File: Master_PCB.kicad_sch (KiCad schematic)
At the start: 15 parts, among them J1 Conn_01x10_Female, J2 Conn_01x04_Female, J214 Conn_01x02_Male, J215 Conn_01x03_Male, J216 Conn_01x02_Male, J220 Conn_01x02_Male, J221 Conn_01x03_Male, J3 Conn_01x06_Female, J4 SJ1-3533NG

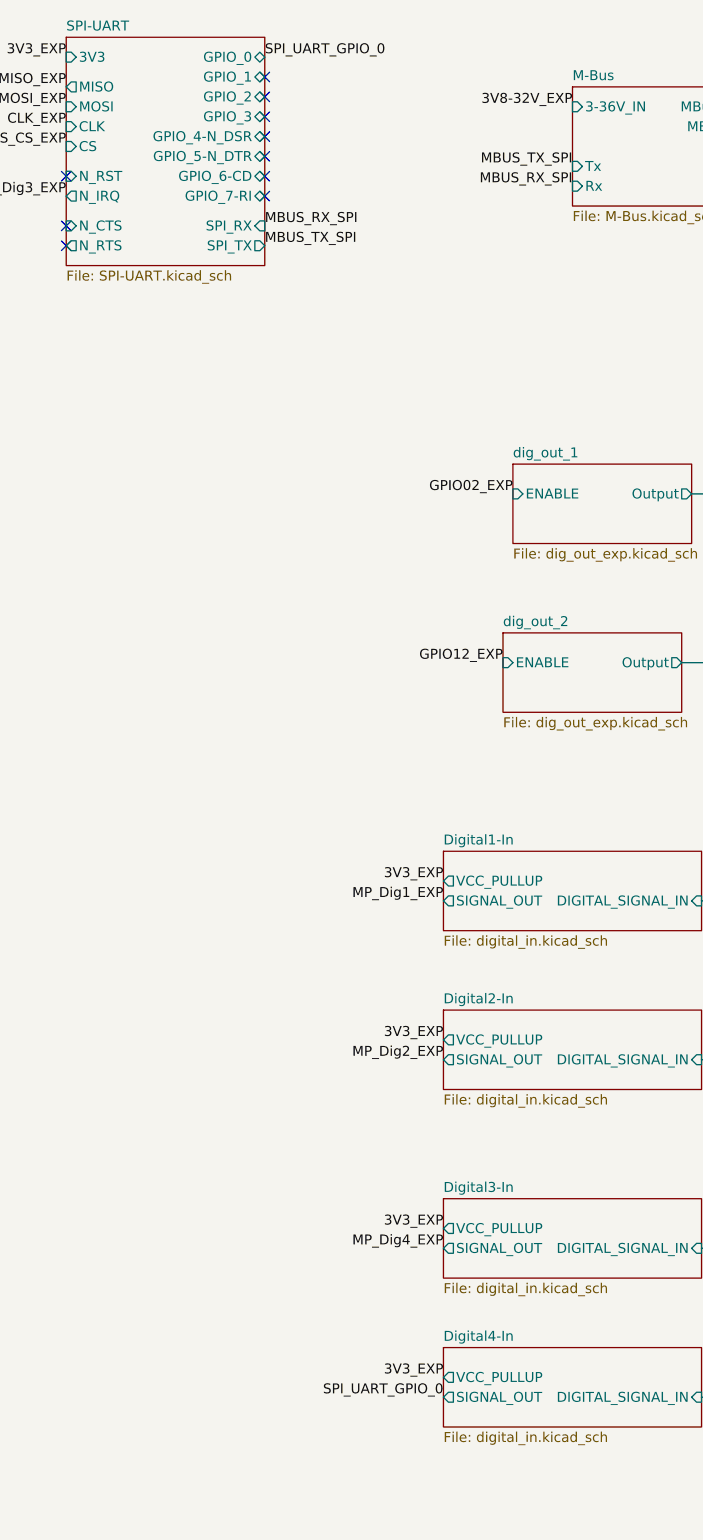
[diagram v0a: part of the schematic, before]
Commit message: changed pin of digital in 1 to a GPIO to be able to handel a serial connection
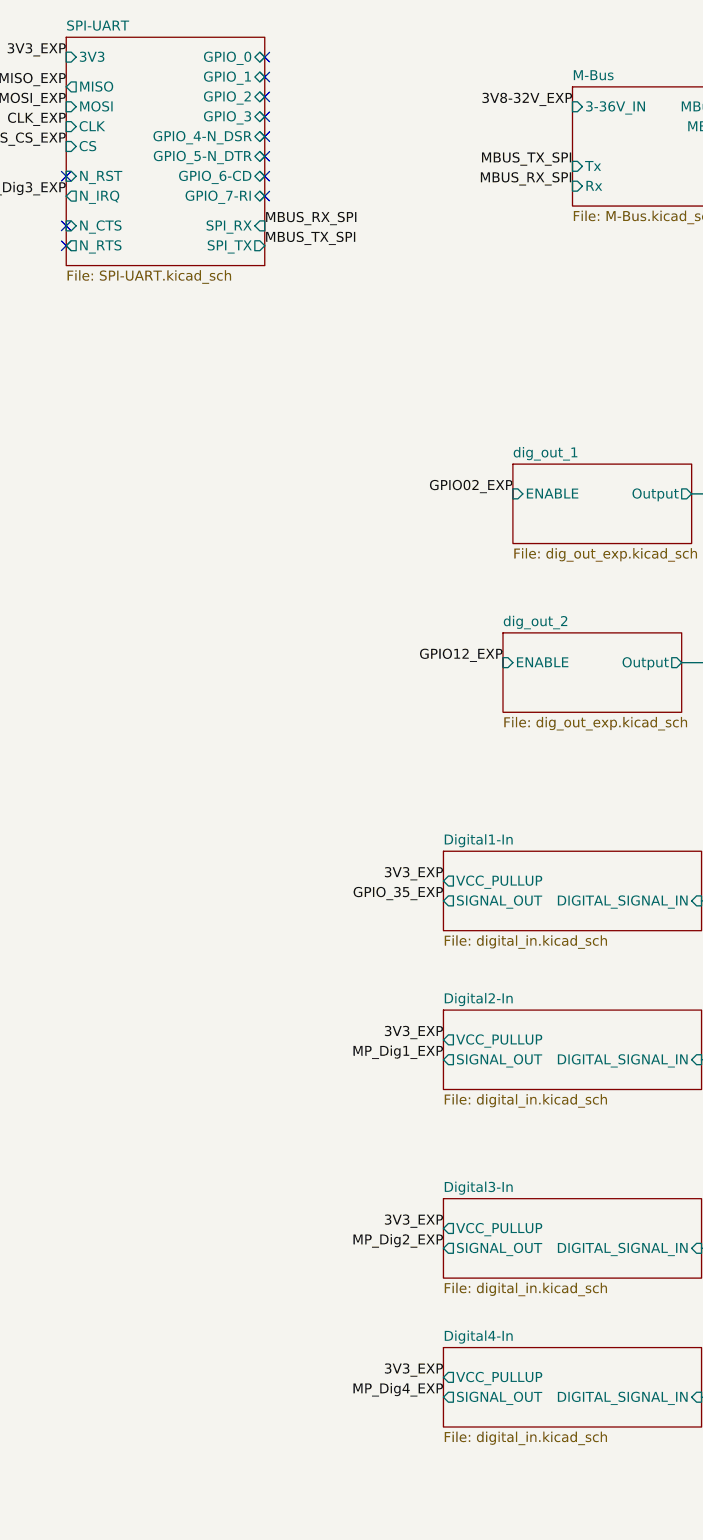
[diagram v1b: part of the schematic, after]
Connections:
- no-connect marks 11 -> 12
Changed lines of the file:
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@@
+	)
+	(no_connect
+		(at 176.53 43.18)
 	)
 	(no_connect
@@
 		)
 	)
+	(label "GPIO_35_EXP"
+		(at 199.39 151.13 180)
+		(effects
+			(font
+				(size 1.27 1.27)
+			)
+			(justify right bottom)
+		)
+	)
 	(label "3V3_EXP"
 		(at 101.6 146.05 0)
@@
 		)
 	)
-	(label "SPI_UART_GPIO_0"
-		(at 199.39 214.63 180)
-		(effects
-			(font
-				(size 1.27 1.27)
-			)
-			(justify right bottom)
-		)
-	)
 	(label "MBUS_RX_SPI"
 		(at 215.9 59.69 180)
@@
 		)
 	)
-	(label "SPI_UART_GPIO_0"
-		(at 176.53 43.18 0)
-		(effects
-			(font
-				(size 1.27 1.27)
-			)
-			(justify left bottom)
-		)
-	)
 	(label "3V3_EXP"
 		(at 199.39 148.59 180)
@@
 	)
 	(label "MP_Dig4_EXP"
-		(at 199.39 195.58 180)
+		(at 199.39 214.63 180)
 		(effects
 			(font
@@
 	)
 	(label "MP_Dig2_EXP"
-		(at 199.39 171.45 180)
+		(at 199.39 195.58 180)
 		(effects
 			(font
@@
 	)
 	(label "MP_Dig1_EXP"
-		(at 199.39 151.13 180)
-		(effects
-			(font
+		(at 199.39 171.45 180)
+		(effects
+			(font
